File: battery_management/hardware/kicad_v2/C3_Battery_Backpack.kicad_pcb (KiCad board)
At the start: 2 copper layers, 13.6 x 18.8 mm, 17 parts, among them P1 P1, P2 P2, P3 P3, P4 P4, P5 P5, P6 P6, P7 P7, Q1 AO3401, U1 TP4054

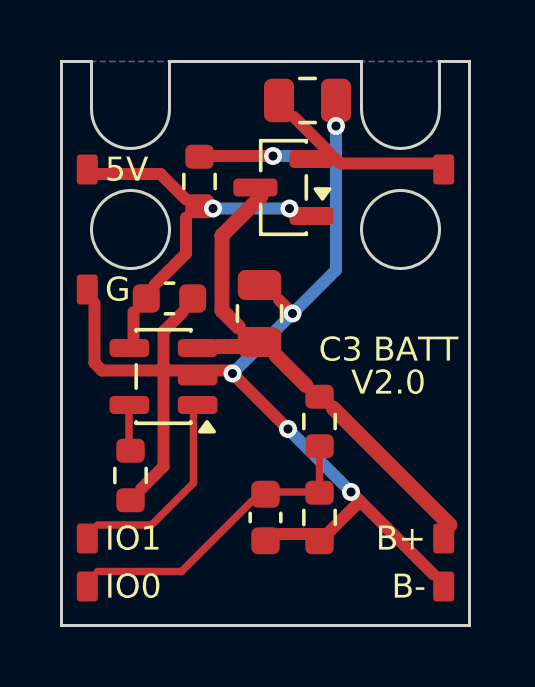
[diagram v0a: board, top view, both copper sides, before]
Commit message: 電池背板 v2.1：取消 USB-C 缺口與圓孔，板子縮為 12.0 × 12.8 mm，並輸出電路圖 PDF/PNG/SVG
- 實板 USB-C 固定腳焊點是平的，geom.py 取消 NOTCHES/HOLES，板框改為矩形
- 零件重排為 4 列，5V/G 接點與排針同高；DRC 0 錯誤、0 未連接
- 新 Gerber：C3_Battery_Backpack_v2.1_Gerber.zip（移除 v2.0 zip）
- 新增 gen_outline.py 產生外形與位置圖，更新 PCB_SPEC 與 KiCad README
- gen_sch.py 修正標題重疊、標籤重疊、PWR_FLAG 超出頁面；版本改為 2.1

Co-Authored-By: Claude Opus 5.5 <noreply@anthropic.com>
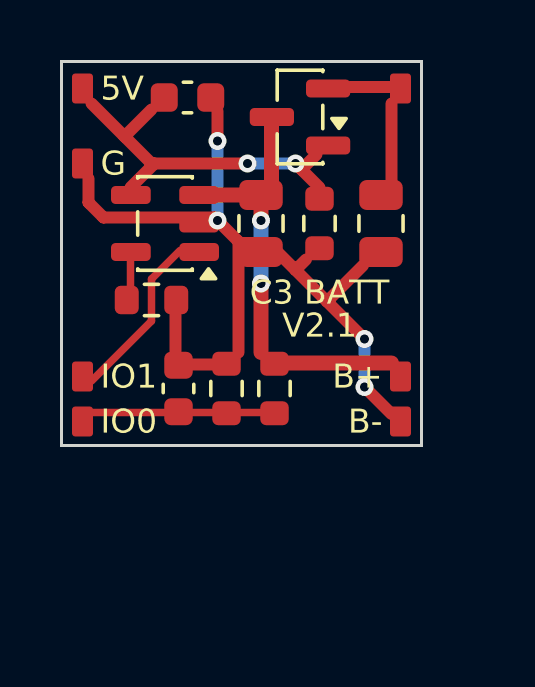
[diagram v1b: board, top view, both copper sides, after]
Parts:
- moved C1 6.73 mm to (104.2, 101.2)
- moved R2 5.89 mm to (103.0, 108.0), turned to 0 degrees
- moved P7 5.69 mm to (111.3, 112.0)
- moved P6 5.59 mm to (111.3, 110.5)
- moved P4 5.50 mm to (100.7, 112.0)
- moved P3 5.40 mm to (100.7, 110.5)
- moved R4 5.30 mm to (105.5, 110.9), turned to 90 degrees
- moved C4 5.19 mm to (103.9, 110.9), turned to 90 degrees
- moved U1 5.10 mm to (103.5, 105.4)
- moved C3 4.78 mm to (110.7, 105.4), turned to -90 degrees
- moved R1 4.24 mm to (108.6, 105.4), turned to -90 degrees
- moved P2 4.20 mm to (100.7, 103.4)
- moved P5 3.06 mm to (111.3, 100.9)
- moved C2 3.00 mm to (106.7, 105.4), turned to -90 degrees
- moved P1 2.70 mm to (100.7, 100.9)
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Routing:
- net GND: track 40.4 -> 26.3 mm, vias 6 -> 4
- net VBUS: track 9.44 -> 11.9 mm
- net VBAT_SENSE: track 7.82 -> 5.65 mm
- net VBAT: track 12.7 -> 10.9 mm, vias 0 -> 2
- net VSYS: track 5.29 -> 4.00 mm
- net CHRG: track 6.08 -> 5.57 mm
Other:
- board size 13.6 x 18.8 mm -> 12 x 12.8 mm
- board text added: "V2.1"
- board text removed: "V2.0"
